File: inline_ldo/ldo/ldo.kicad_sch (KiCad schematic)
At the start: 1 part, among them U1 LT3045xDD

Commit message: pushes
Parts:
- added C1, C2: 10u, symbol Device:C
- added C3: C, symbol Device:C
- added J1: Conn_01x03_Socket, Connector_JST:JST_EH_S3B-EH_1x03_P2.50mm_Horizontal, symbol Connector:Conn_01x03_Socket
- added J2: USB_A, Connector_USB:USB_A_Molex_48037-2200_Horizontal, symbol Connector:USB_A
- added J3: USB_C_Receptacle_USB2.0_16P, Connector_USB:USB_C_Receptacle_GCT_USB4110, symbol Connector:USB_C_Receptacle_USB2.0_16P
- added R1, R2: 5.1k, Capacitor_SMD:C_0603_1608Metric, symbol Device:R
- added U1: USBLC6-2SC6, Package_TO_SOT_SMD:SOT-23-6, symbol Power_Protection:USBLC6-2SC6
- renumbered U1 to U2
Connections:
- net at U2.1 (IN), U2.2 (IN): now also C1.1
- net at U2.10 (OUT): now also C2.1
- net GND: now reaches U2.11 (GND), U2.8 (GND)
- net GND: now also C1.2, C2.2, C3.2, J3.A1 (GND), J3.A12 (GND), J3.B1 (GND), J3.B12 (GND), R1.2, R2.2, U1.2 (GND)
- new net: J3.A6 (D+), J3.B6 (D+), U1.3 (I/O2)
- new net: J3.A7 (D-), J3.B7 (D-), U1.1 (I/O1)
- new net: C3.1, J3.S1 (SHIELD)
- new net D+: J2.3 (D+), U1.4 (I/O2)
- new net D-: J2.2 (D-), U1.6 (I/O1)
- new net USB_CC1: J3.A5 (CC1), R1.1
- new net USB_CC2: J3.B5 (CC2), R2.1
- new net VBUS: J3.A4 (VBUS), J3.A9 (VBUS), J3.B4 (VBUS), J3.B9 (VBUS), U1.5 (VBUS)
- no-connect marks 0 -> 2
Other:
- note added: "X7R"
- moved on the sheet: U2

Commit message: ldo
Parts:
- removed J1: Conn_01x03_Socket, Connector_JST:JST_EH_S3B-EH_1x03_P2.50mm_Horizontal, symbol Connector:Conn_01x03_Socket
- added C4: 100n, symbol Device:C
- added C5: C, symbol Device:C
- added R3, R4, R5, R6: 5.1k, Capacitor_SMD:C_0603_1608Metric, symbol Device:R
- C3: value C -> 100n
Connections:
- net GND: now also J2.4 (GND), C4.2, C5.2, R3.2, R4.2, R6.2
- net VBUS: no longer J3.A4 (VBUS), J3.A9 (VBUS), J3.B4 (VBUS), J3.B9 (VBUS)
- net at J3.A6 (D+), J3.B6 (D+): now also J2.3 (D+); no longer U1.3 (I/O2)
- net at J3.A7 (D-), J3.B7 (D-): now also J2.2 (D-); no longer U1.1 (I/O1)
- net 5V: now reaches C2.1, U2.10 (OUT)
- net 5V: now also J2.1 (VBUS), U2.9 (OUTS), R5.1
- net VIN: now reaches C1.1, U2.1 (IN), U2.2 (IN)
- net VIN: now also J3.A4 (VBUS), J3.A9 (VBUS), J3.B4 (VBUS), J3.B9 (VBUS), U2.3 (EN/UV)
- net at U2.5 (ILIM): now also R3.1
- net at U2.6 (PGFB): now also R4.1, R5.2
- net at U2.7 (SET): now also C5.1, R6.1
- net at J2.5 (Shield): now also C4.1
- net D+: no longer names the net of U1.4 (I/O2)
- net D+: no longer J2.3 (D+)
- net D-: no longer names the net of U1.6 (I/O1)
- net D-: no longer J2.2 (D-)
- no-connect marks 2 -> 3
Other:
- moved on the sheet: C1, C2, J2, R1, R2, U2

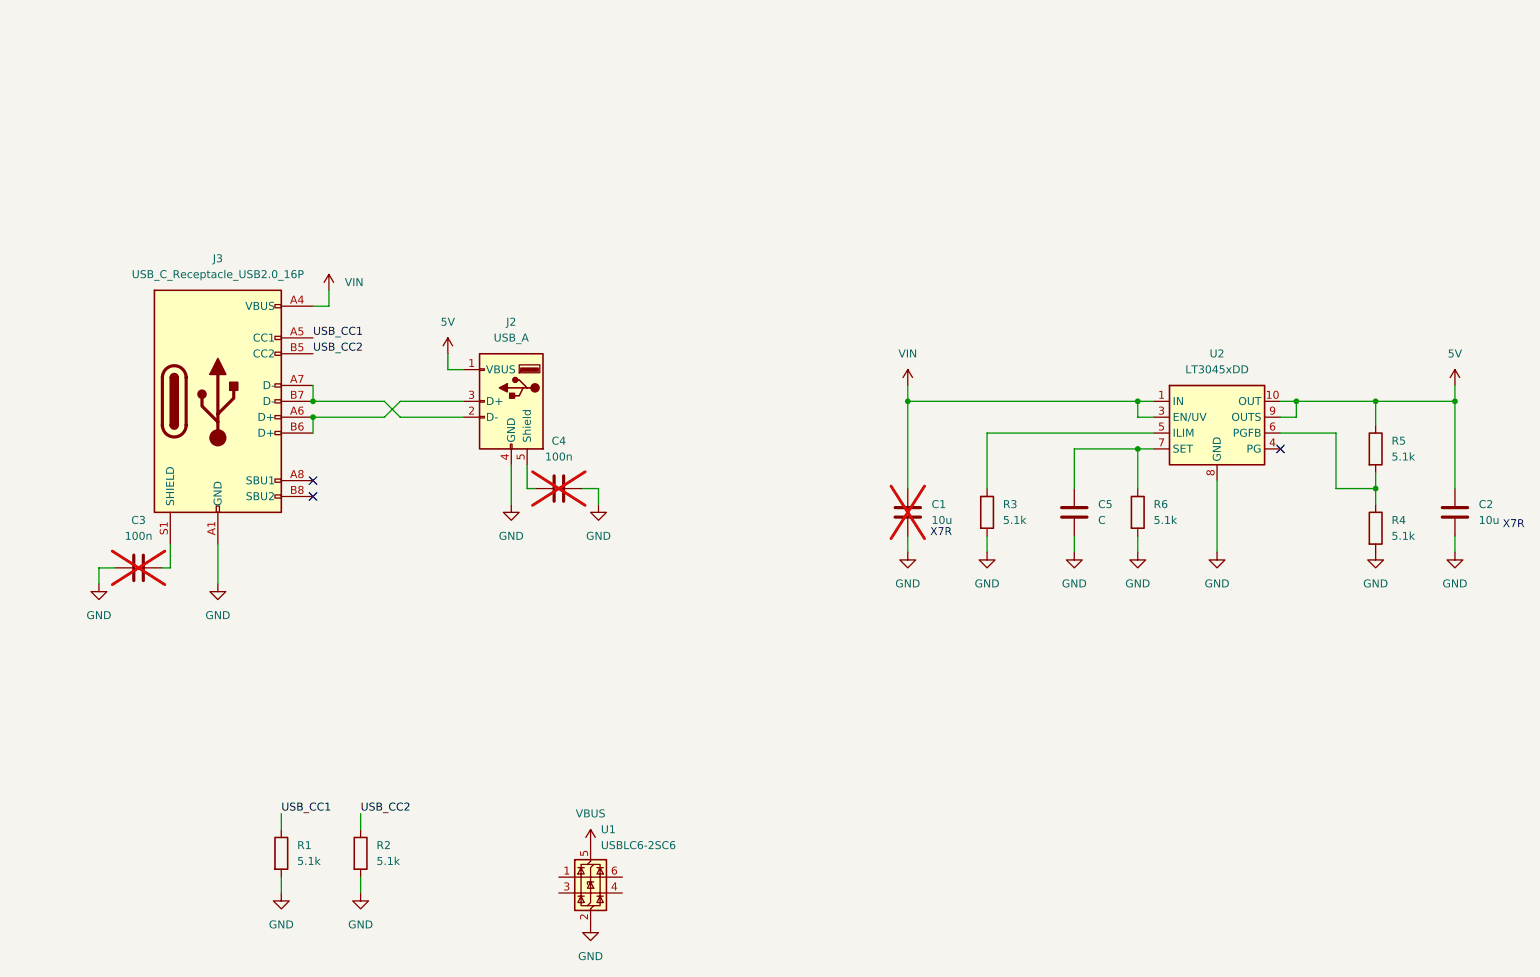
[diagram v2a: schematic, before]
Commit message: more work on inline ldo
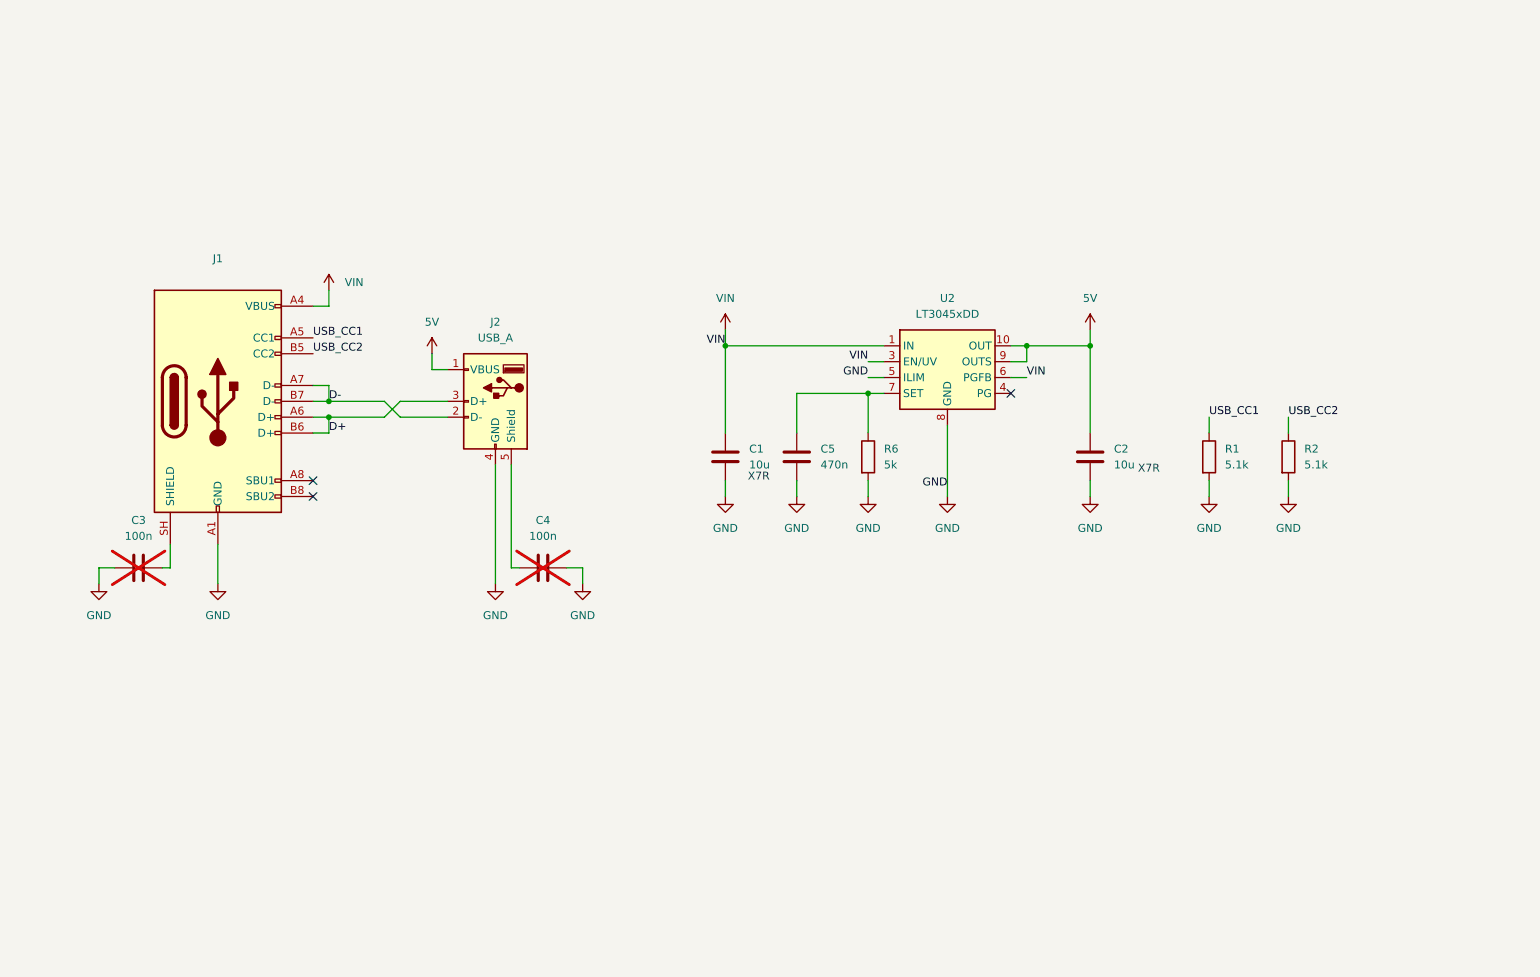
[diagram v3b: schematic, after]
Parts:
- removed J3: USB_C_Receptacle_USB2.0_16P, Connector_USB:USB_C_Receptacle_GCT_USB4110, symbol Connector:USB_C_Receptacle_USB2.0_16P
- removed R3, R4, R5: 5.1k, Capacitor_SMD:C_0603_1608Metric, symbol Device:R
- removed U1: USBLC6-2SC6, Package_TO_SOT_SMD:SOT-23-6, symbol Power_Protection:USBLC6-2SC6
- added J1: (no value), Connector_USB:USB_C_Receptacle_GCT_USB4110, symbol Connector:USB_C_Receptacle_USB2.0_16P
- C1: footprint (none) -> Capacitor_SMD:C_0603_1608Metric; now fitted
- C2: footprint (none) -> Capacitor_SMD:C_0603_1608Metric
- C3, C4: footprint (none) -> Capacitor_SMD:C_0402_1005Metric
- C5: value C -> 470n; footprint (none) -> Capacitor_SMD:C_0402_1005Metric
- J2: footprint Connector_USB:USB_A_Molex_48037-2200_Horizontal -> Connector_USB:USB_A_Receptacle_GCT_USB1046
- R1, R2: footprint Capacitor_SMD:C_0603_1608Metric -> Capacitor_SMD:C_0402_1005Metric
- R6: value 5.1k -> 5k; footprint Capacitor_SMD:C_0603_1608Metric -> Capacitor_SMD:C_0402_1005Metric
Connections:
- net GND: now also U2.5 (ILIM), J1.A1 (GND), J1.A12 (GND), J1.B1 (GND), J1.B12 (GND)
- net USB_CC1: now also J1.A5 (CC1)
- net USB_CC2: now also J1.B5 (CC2)
- net VIN: now also U2.6 (PGFB), J1.A4 (VBUS), J1.A9 (VBUS), J1.B4 (VBUS), J1.B9 (VBUS)
- net D+: now reaches J2.3 (D+)
- net D+: now also J1.A6 (D+), J1.B6 (D+)
- net D-: now reaches J2.2 (D-)
- net D-: now also J1.A7 (D-), J1.B7 (D-)
- net at C3.1: now also J1.SH (SHIELD)
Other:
- moved on the sheet: C2, C4, C5, J2, R1, R2, R6, U2

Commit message: almost finished hopefully
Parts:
- added TP1, TP2: TestPoint, TestPoint:TestPoint_Pad_D1.0mm, symbol Connector:TestPoint
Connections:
- net 5V: now also TP2.1
- net VIN: now also TP1.1
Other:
- moved on the sheet: C4, J2, R1, R2

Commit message: pushes
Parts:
- removed TP1, TP2: TestPoint, TestPoint:TestPoint_Pad_D1.0mm, symbol Connector:TestPoint
- added D1: SBR3U60P1-7, Diode_SMD:D_PowerDI-123, symbol Device:D_Schottky
- added R7, R8: 1M, Capacitor_SMD:C_0402_1005Metric, symbol Device:R
- C3, C4: now fitted
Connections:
- net 5V: now also D1.1 (K)
- net GND: now also R7.2, R8.1
- net VIN: now also D1.2 (A)
- net at C4.1, J2.5 (Shield): now also R8.2
- net at C3.1, J1.SH (SHIELD): now also R7.1

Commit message: minor
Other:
- note removed: "X7R"
- moved on the sheet: C1, C2, C3, C4, C5, D1, J1, J2, R1, R2, R6, R7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

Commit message: minor
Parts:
- R6: value 5k -> 50k
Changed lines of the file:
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@@
 			)
 		)
-		(property "Value" "5k"
+		(property "Value" "50k"
 			(at 144.78 67.3099 0)
 			(show_name no)
